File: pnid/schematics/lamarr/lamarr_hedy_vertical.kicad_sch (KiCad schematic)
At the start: 94 parts, among them U1 Rocket_Big

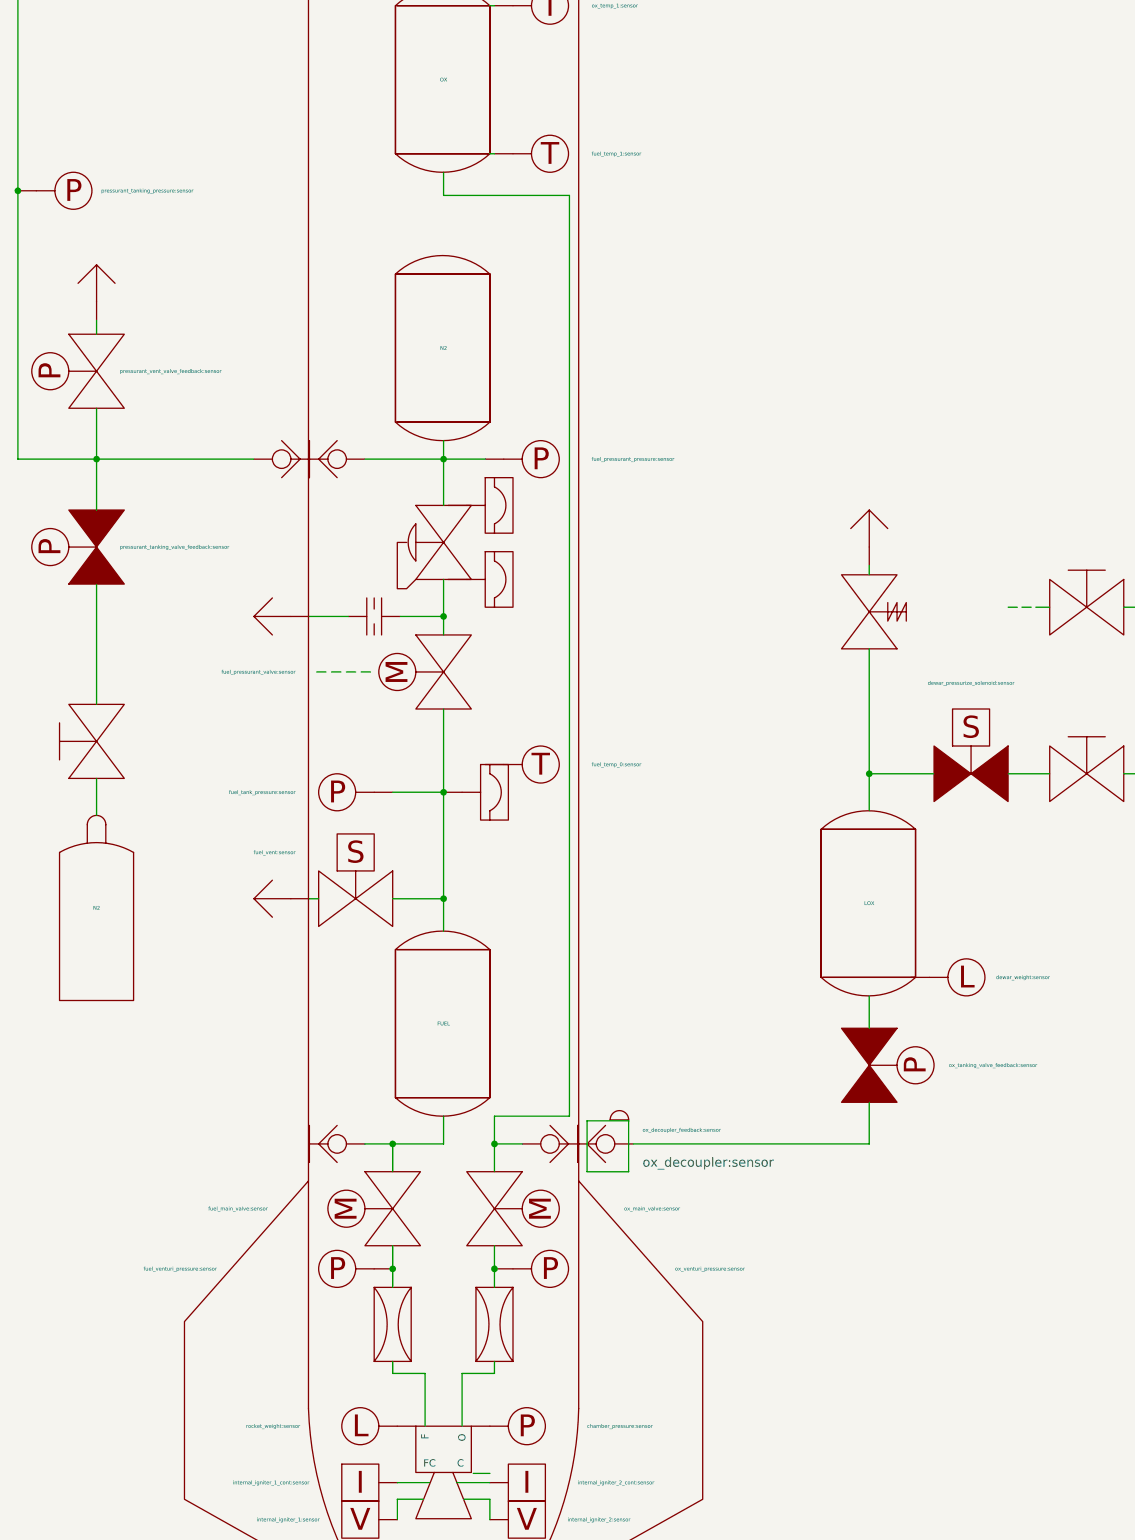
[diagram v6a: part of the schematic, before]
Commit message: added temperature sensors to vertical hedy PnID (to be tested)
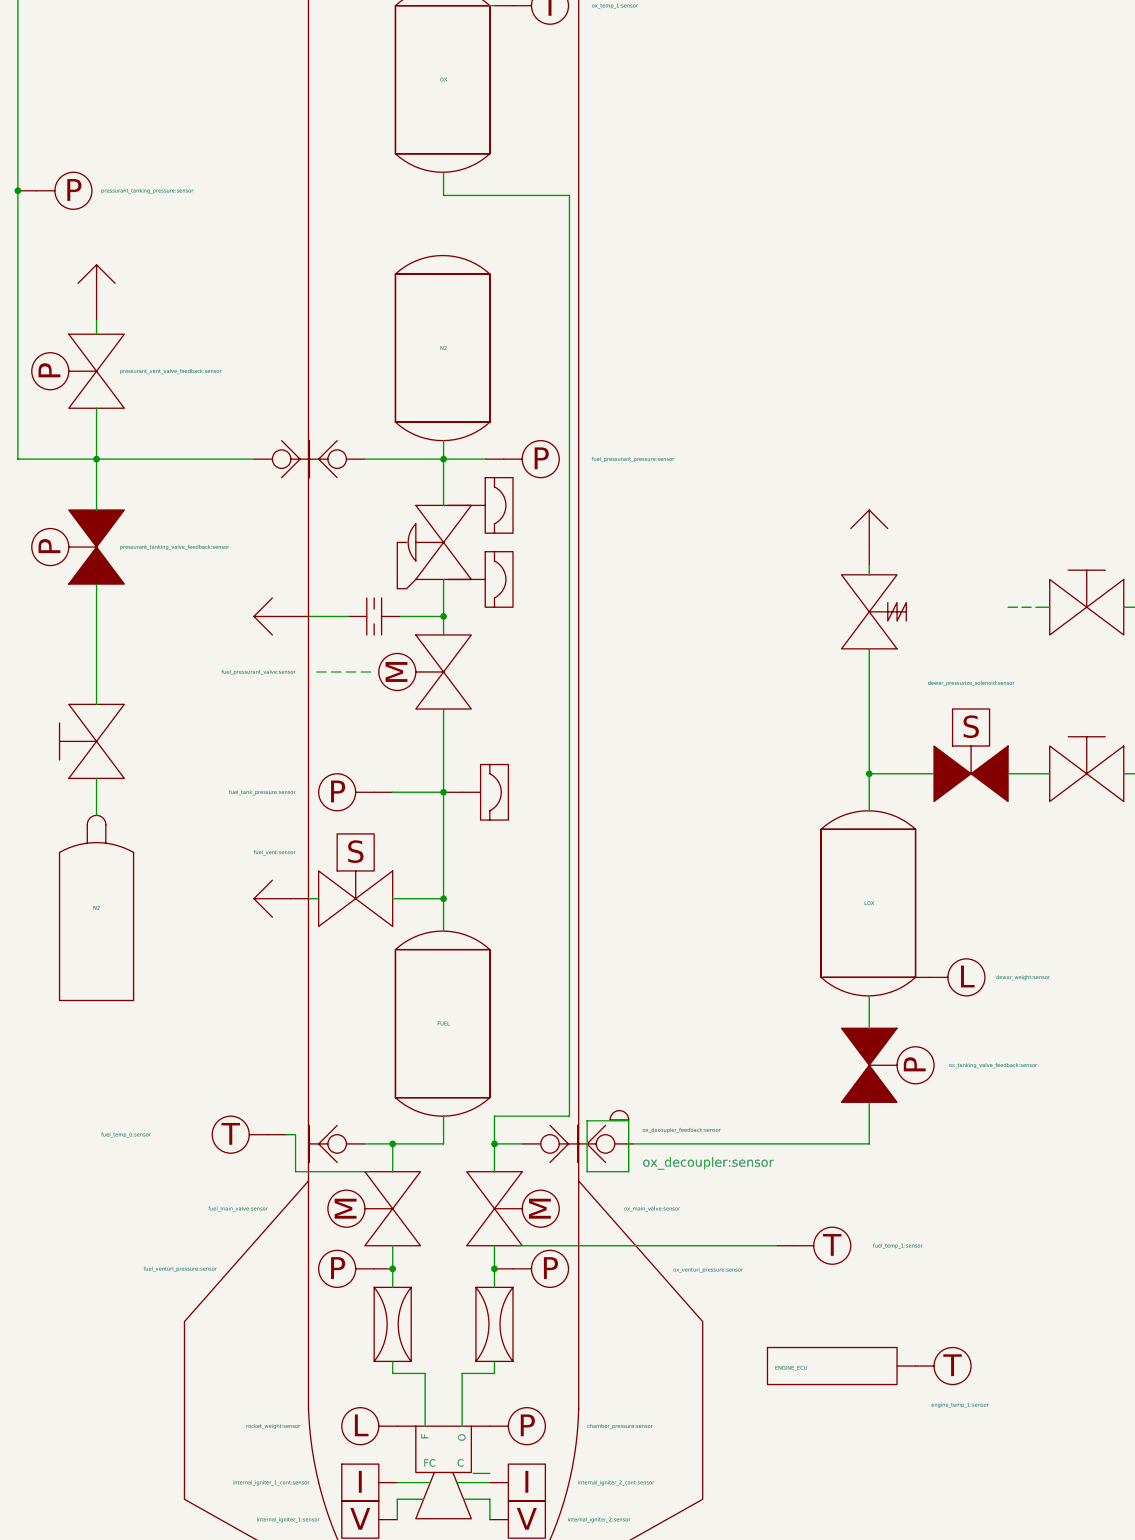
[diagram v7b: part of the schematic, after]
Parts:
- added engine_ECU_temperature1: engine_temp_1:sensor, symbol PnID-Lib:Sensor_Temperature
- added engineecu1: ENGINE_ECU, symbol PnID:Label
- renumbered ox_manifold_temperature to burst_disk_temperature, ox_tank_bottom_temperature to ox_main_valve_servo_temperature
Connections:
- net at engine.~ (O): now also venturi1.~
- net at ox_venturi.~: now also ox_main_valve.~, ox_venturi_pressure.~; no longer engine.~ (O)
- net at venturi1.~: now also fuel_main_valve.~, fuel_venturi_pressure.~; no longer engine.~ (O)
- net at dewar_needle_valve?.~: now also C2.~, C3.~; no longer C1.~
- new net: engine.~ (O), ox_venturi.~
- new net: OX.~, ox_main_valve.~, ox_quick_connect.~
- new net: DewarOverPressureValve?.~, LOX.~, dewar_pressurize_solenoid.~
- new net: C1.~, dewar_needle_valve?.~
- new net: Orifice1.~, ox_pressurant_valve.~, pressurantPressureRegulator2.~
- new net: FUEL.~, fuel_main_valve.~, ox_quick_connect1.~
- new net: Orifice2.~, fuel_pressurant_valve.~, pressurantPressureRegulator1.~
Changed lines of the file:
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@@
 	(wire
 		(pts
-			(xy 73.66 -2.54) (xy 74.295 -2.54)
+			(xy 81.407 -60.96) (xy 82.677 -60.96)
 		)
 		(stroke
@@
 	(wire
 		(pts
-			(xy 81.407 -60.96) (xy 82.677 -60.96)
+			(xy 56.515 -90.17) (xy 67.31 -90.17)
 		)
 		(stroke
@@
 	(wire
 		(pts
-			(xy 56.515 -90.17) (xy 67.31 -90.17)
+			(xy 67.31 -31.115) (xy 67.31 -25.4)
 		)
 		(stroke
@@
 	(wire
 		(pts
-			(xy 67.31 -31.115) (xy 67.31 -25.4)
+			(xy 67.31 -73.66) (xy 67.31 -68.58)
 		)
 		(stroke
@@
 	(wire
 		(pts
-			(xy 67.31 -73.66) (xy 67.31 -68.58)
+			(xy 46.99 137.16) (xy 57.15 137.16)
 		)
 		(stroke
@@
 	(wire
 		(pts
+			(xy 45.72 132.08) (xy 46.99 132.08)
+		)
+		(stroke
+			(width 0)
+			(type default)
+		)
+	)
+	(wire
+		(pts
 			(xy 19.685 39.37) (xy 41.275 39.37)
 		)
@@
 	(wire
 		(pts
+			(xy 77.47 147.32) (xy 113.03 147.32)
+		)
+		(stroke
+			(width 0)
+			(type default)
+		)
+	)
+	(wire
+		(pts
+			(xy 46.99 132.08) (xy 46.99 137.16)
+		)
+		(stroke
+			(width 0)
+			(type default)
+		)
+	)
+	(wire
+		(pts
 			(xy 56.007 68.58) (xy 57.277 68.58)
 		)
@@
 		(on_board yes)
 		(dnp no)
-		(property "Reference" "ox_manifold_temperature"
+		(property "Reference" "burst_disk_temperature"
 			(at 85.725 -48.895 0)
 			(effects
@@
 			(project "lamarr_hedy_vertical"
 				(path "/604fc9f3-63a6-4133-afd1-4a5c2507dc1d"
-					(reference "ox_manifold_temperature")
+					(reference "burst_disk_temperature")
 					(unit 1)
 				)
@@
 	)
 	(symbol
+		(lib_name "Label_4")
+		(lib_id "PnID:Label")
+		(at 119.38 163.83 0)
+		(unit 1)
+		(exclude_from_sim no)
+		(in_bom yes)
+		(on_board yes)
+		(dnp no)
+		(property "Reference" "engineecu1"
+			(at 119.38 158.242 0)
+			(effects
+				(font
+					(size 1.27 1.27)
+				)
+				(hide yes)
+			)
+		)
+		(property "Value" "ENGINE_ECU"
+			(at 112.776 164.084 0)
+			(effects
+				(font
+					(size 0.508 0.508)
+				)
+				(justify left)
+			)
+		)
+		(property "Footprint" ""
+			(at 119.38 163.83 0)
+			(effects
+				(font
+					(size 1.27 1.27)
+				)
+				(hide yes)
+			)
+		)
+		(property "Datasheet" ""
+			(at 119.38 163.83 0)
+			(effects
+				(font
+					(size 1.27 1.27)
+				)
+				(hide yes)
+			)
+		)
+		(property "Description" ""
+			(at 119.38 163.83 0)
+			(effects
+				(font
+					(size 1.27 1.27)
+				)
+				(hide yes)
+			)
+		)
+		(instances
+			(project "lamarr_hedy_vertical"
+				(path "/604fc9f3-63a6-4133-afd1-4a5c2507dc1d"
+					(reference "engineecu1")
+					(unit 1)
+				)
+			)
+		)
+	)
+	(symbol
+		(lib_id "PnID-Lib:Sensor_Temperature")
+		(at 137.16 163.83 0)
+		(unit 1)
+		(exclude_from_sim no)
+		(in_bom yes)
+		(on_board yes)
+		(dnp no)
+		(property "Reference" "engine_ECU_temperature1"
+			(at 140.97 163.195 0)
+			(effects
+				(font
+					(size 0.508 0.508)
+				)
+				(justify left)
+				(hide yes)
+			)
+		)
+		(property "Value" "engine_temp_1:sensor"
+			(at 134.239 169.164 0)
+			(effects
+				(font
+					(size 0.508 0.508)
+				)
+				(justify left)
+			)
+		)
+		(property "Footprint" ""
+			(at 137.16 163.83 0)
+			(effects
+				(font
+					(size 0.508 0.508)
+				)
+				(hide yes)
+			)
+		)
+		(property "Datasheet" ""
+			(at 137.16 163.83 0)
+			(effects
+				(font
+					(size 0.508 0.508)
+				)
+				(hide yes)
+			)
+		)
+		(property "Description" ""
+			(at 137.16 163.83 0)
+			(effects
+				(font
+					(size 1.27 1.27)
+				)
+				(hide yes)
+			)
+		)
+		(property "Unit" "˚C"
+			(at 137.16 163.83 0)
+			(effects
+				(font
+					(size 0.508 0.508)
+				)
+				(hide yes)
+			)
+		)
+		(property "Action_Reference" " "
+			(at 137.16 163.83 0)
+			(effects
+				(font
+					(size 1.27 1.27)
+				)
+				(hide yes)
+			)
+		)
+		(pin "~"
+		)
+		(instances
+			(project "lamarr_hedy_vertical"
+				(path "/604fc9f3-63a6-4133-afd1-4a5c2507dc1d"
+					(reference "engine_ECU_temperature1")
+					(unit 1)
+				)
+			)
+		)
+	)
+	(symbol
 		(lib_id "PnID-Lib:Valve_Servo")
 		(at 74.295 142.24 270)
@@
 		)
 		(property "Value" "ox_venturi_pressure:sensor"
-			(at 99.06 150.495 0)
+			(at 98.806 150.622 0)
 			(effects
 				(font
@@
 	(symbol
 		(lib_id "PnID-Lib:Sensor_Temperature")
-		(at 81.915 -2.54 0)
+		(at 120.65 147.32 0)
 		(unit 1)
 		(exclude_from_sim no)
@@
 		(on_board yes)
 		(dnp no)
-		(property "Reference" "ox_tank_bottom_temperature"
-			(at 85.725 -3.175 0)
+		(property "Reference" "ox_main_valve_servo_temperature"
+			(at 124.46 146.685 0)
 			(effects
 				(font
@@
 		)
 		(property "Value" "fuel_temp_1:sensor"
-			(at 87.63 -2.54 0)
+			(at 126.238 147.32 0)
 			(effects
 				(font
@@
 		)
 		(property "Footprint" ""
-			(at 81.915 -2.54 0)
+			(at 120.65 147.32 0)
 			(effects
 				(font
@@
 		)
 		(property "Datasheet" ""
-			(at 81.915 -2.54 0)
+			(at 120.65 147.32 0)
 			(effects
 				(font
@@
 		)
 		(property "Description" ""
-			(at 81.915 -2.54 0)
+			(at 120.65 147.32 0)
 			(effects
 				(font
@@
 		)
 		(property "Unit" "˚C"
-			(at 81.915 -2.54 0)
+			(at 120.65 147.32 0)
 			(effects
 				(font
@@
 		)
 		(property "Action_Reference" " "
-			(at 81.915 -2.54 0)
+			(at 120.65 147.32 0)
 			(effects
 				(font
@@
 			(project ""
 				(path "/604fc9f3-63a6-4133-afd1-4a5c2507dc1d"
-					(reference "ox_tank_bottom_temperature")
+					(reference "ox_main_valve_servo_temperature")
 					(unit 1)
 				)
@@
 	)
 	(symbol
+		(lib_name "Sensor_Temperature_1")
 		(lib_id "PnID-Lib:Sensor_Temperature")
-		(at 80.645 81.28 0)
+		(at 40.64 132.08 0)
 		(unit 1)
 		(exclude_from_sim no)
@@
 		(dnp no)
 		(property "Reference" "fuel_manifold_temperature"
-			(at 84.455 80.645 0)
+			(at 24.638 131.318 0)
 			(effects
 				(font
@@
 		)
 		(property "Value" "fuel_temp_0:sensor"
-			(at 87.63 81.28 0)
+			(at 20.32 132.08 0)
 			(effects
 				(font
@@
 		)
 		(property "Footprint" ""
-			(at 80.645 81.28 0)
+			(at 38.1 132.08 0)
 			(effects
 				(font
@@
 		)
 		(property "Datasheet" ""
-			(at 80.645 81.28 0)
+			(at 38.1 132.08 0)
 			(effects
 				(font
@@
 		)
 		(property "Description" ""
-			(at 80.645 81.28 0)
+			(at 38.1 132.08 0)
 			(effects
 				(font
@@
 		)
 		(property "Unit" "˚C"
-			(at 80.645 81.28 0)
+			(at 38.1 132.08 0)
 			(effects
 				(font
@@
 		)
 		(property "Action_Reference" " "
-			(at 80.645 81.28 0)
+			(at 38.1 132.08 0)
 			(effects
 				(font

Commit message: updated PNID
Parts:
- removed fuel_manifold_temperature: fuel_temp_0:sensor, symbol PnID-Lib:Sensor_Temperature
- added Green: gse_elec_bob_lamp_green:sensor, symbol PnID-Lib:LED
- added Red: gse_elec_bob_lamp_red:sensor, symbol PnID-Lib:LED
- added Safety: safety_light, symbol PnID-Lib:Flowchart_State
- added dewar_pressure: dewar_pressure:sensor, symbol PnID-Lib:Sensor_Pressure
- added ox_decoupler_temperature1: ox_temp_0:sensor, symbol PnID-Lib:Sensor_Temperature
- added press_in: press_in:sensor, symbol PnID-Lib:Sensor_Pressure
- added ventilinsel_pressure: ventilinsel_pressure:sensor, symbol PnID-Lib:Sensor_Pressure
- engine_ECU_temperature: renamed from engine_ECU_temperature1; value engine_temp_1:sensor -> engine_temp_0:sensor
- ox_decoupler_temperature: renamed from burst_disk_temperature; value ox_temp_0:sensor -> engine_temp_1:sensor
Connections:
- net at engine.~ (C): now also venturi1.~
- net at ox_venturi.~: now also ox_main_valve.~, ox_venturi_pressure.~; no longer engine.~ (O)
- net at venturi1.~: now also fuel_main_valve.~, fuel_venturi_pressure.~; no longer engine.~ (O)
- net at C4.~, dewar_pressurize_solenoid.~: now also dewar_pressure.~
- net at dewar_needle_valve?.~: now also C2.~, C3.~, press_in.~; no longer C1.~
- net at C5.~: now also ventilinsel_pressure.~
- new net: engine.~ (C), ox_venturi.~
- new net: OX.~, ox_main_valve.~, ox_quick_connect.~
- new net: DewarOverPressureValve?.~, LOX.~, dewar_pressurize_solenoid.~
- new net: C1.~, dewar_needle_valve?.~
- new net: N2.~, ox_decoupler_temperature1.~
- new net: Orifice1.~, ox_pressurant_valve.~, pressurantPressureRegulator2.~
- new net: FUEL.~, fuel_main_valve.~, ox_quick_connect1.~
- new net: Orifice2.~, fuel_pressurant_valve.~, pressurantPressureRegulator1.~
